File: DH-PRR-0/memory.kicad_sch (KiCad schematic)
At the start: 8 parts, among them J2 Micro_SD_Card_Det2, J4 USB_A, U8 MCP2210x-MQ

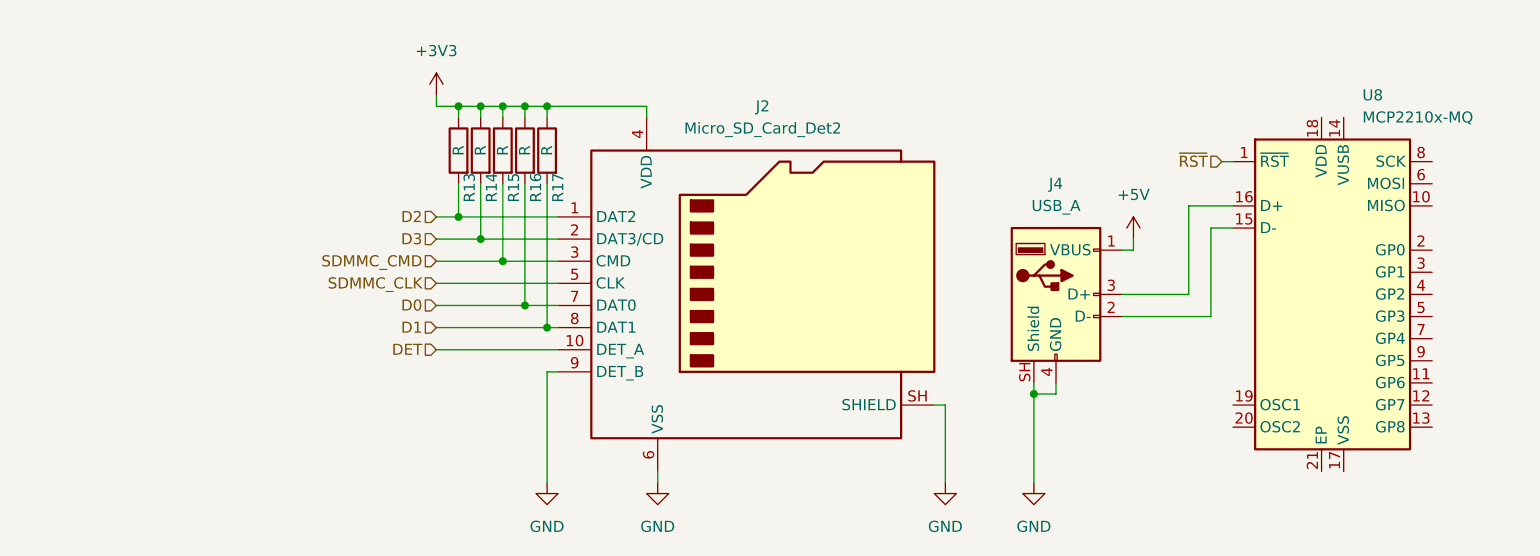
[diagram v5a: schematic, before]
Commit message: changed usb-spi bridge to host bridge, now functional
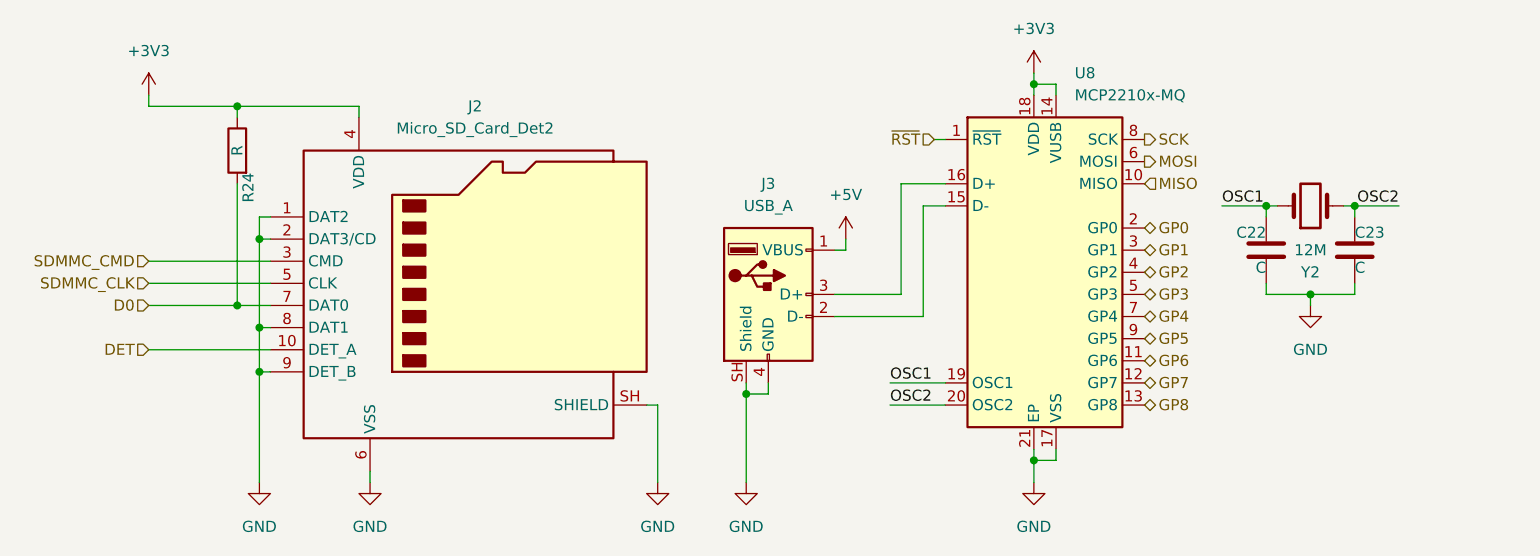
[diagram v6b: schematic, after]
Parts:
- removed R13, R14, R15, R17: R, symbol Device:R
- added C22, C23: C, symbol Device:C
- added Y2: 12M, symbol Device:Crystal
- renumbered J4 to J3, R16 to R24
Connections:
- net D1 is gone; now on net GND: J2.8 (DAT1)
- net D2 is gone; now on net GND: J2.1 (DAT2)
- net D3 is gone; now on net GND: J2.2 (DAT3/CD)
- net +3V3: now also U8.14 (VUSB), U8.18 (VDD)
- net GND: now also U8.17 (VSS), U8.21 (EP), C22.2, C23.2
- net MISO: now reaches U8.10 (MISO)
- net GP6: now reaches U8.11 (GP6)
- net GP7: now reaches U8.12 (GP7)
- net GP8: now reaches U8.13 (GP8)
- net OSC1: now reaches U8.19 (OSC1)
- net OSC1: now also C22.1, Y2.1
- net GP0: now reaches U8.2 (GP0)
- net OSC2: now reaches U8.20 (OSC2)
- net OSC2: now also C23.1, Y2.2
- net GP1: now reaches U8.3 (GP1)
- net GP2: now reaches U8.4 (GP2)
- net GP3: now reaches U8.5 (GP3)
- net MOSI: now reaches U8.6 (MOSI)
- net GP4: now reaches U8.7 (GP4)
- net SCK: now reaches U8.8 (SCK)
- net GP5: now reaches U8.9 (GP5)
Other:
- moved on the sheet: J2, J3, R24, U8
